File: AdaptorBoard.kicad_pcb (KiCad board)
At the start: 2 copper layers, 53.6 x 68.8 mm, 14 parts, among them J1 Conn_02x05_Odd_Even

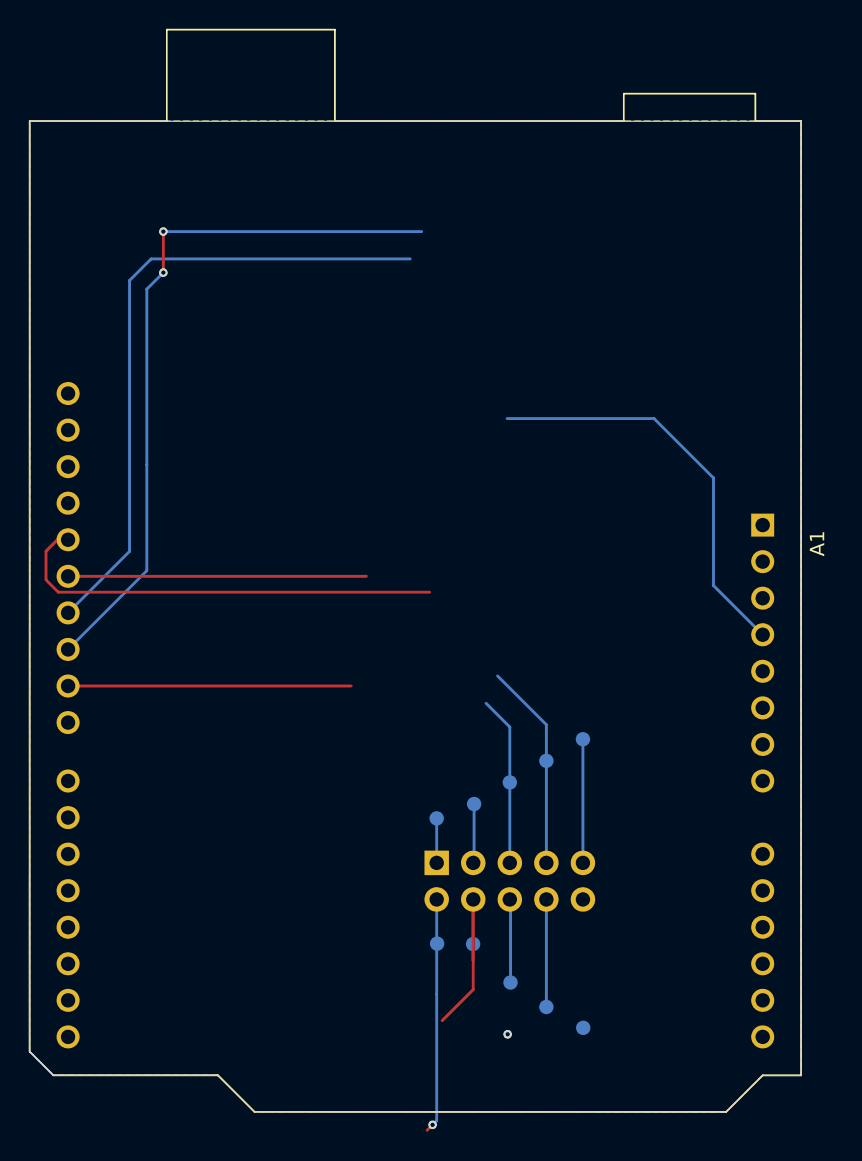
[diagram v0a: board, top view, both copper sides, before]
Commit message: Add EEPROM. Change from Reset Push to input. Assign footprints and more improvements.
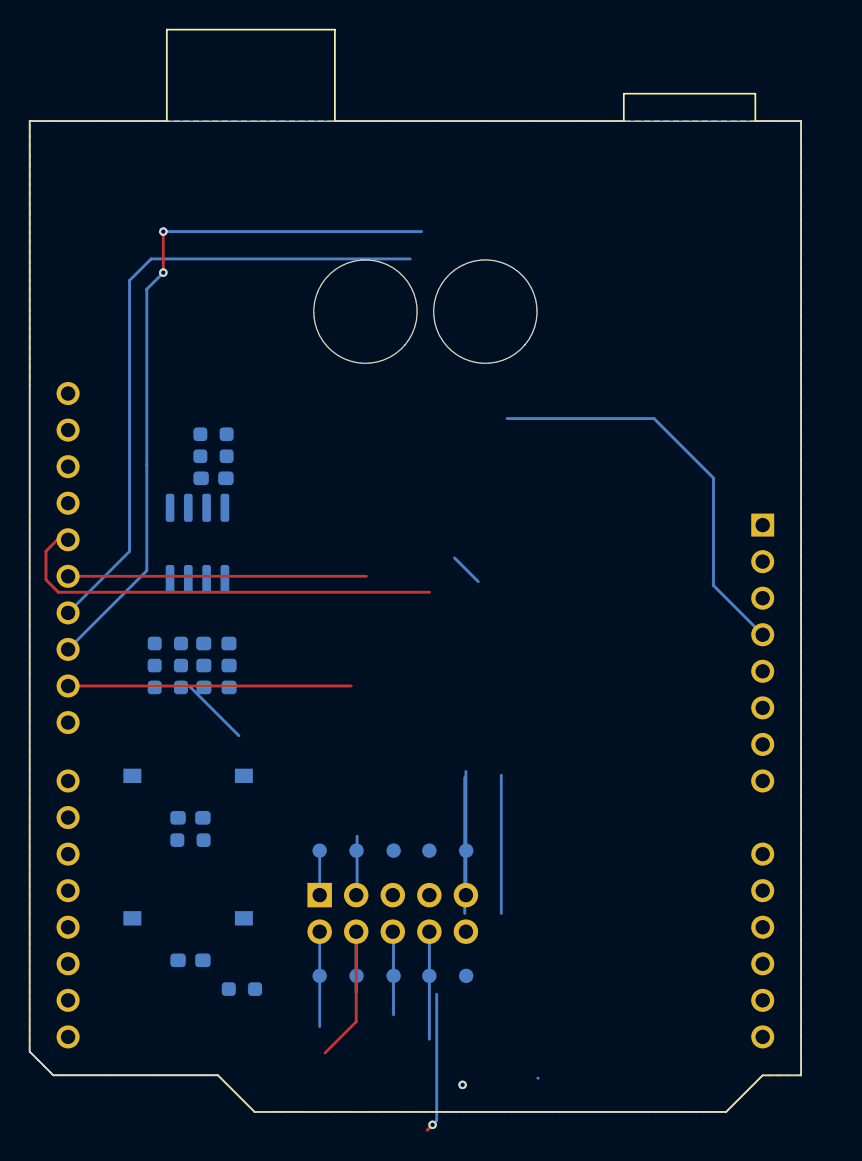
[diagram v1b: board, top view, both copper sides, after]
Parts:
- added C1: 100nF, Capacitor_SMD:C_0603_1608Metric_Pad1.08x0.95mm_HandSolder, B.Cu at (140.7, 130.3)
- added C2: 100nF, Capacitor_SMD:C_0603_1608Metric_Pad1.08x0.95mm_HandSolder, B.Cu at (140.7, 140.2)
- added C3: 100nF, Capacitor_SMD:C_0603_1608Metric_Pad1.08x0.95mm_HandSolder, B.Cu at (142.3, 106.7)
- added D1: LED, LED_SMD:LED_0603_1608Metric_Pad1.05x0.95mm_HandSolder, B.Cu at (142.5, 118.2)
- added D2: LED, LED_SMD:LED_0603_1608Metric_Pad1.05x0.95mm_HandSolder, B.Cu at (142.5, 119.8)
- added D3: LED, LED_SMD:LED_0603_1608Metric_Pad1.05x0.95mm_HandSolder, B.Cu at (142.5, 121.3)
- added R1: 1K, Resistor_SMD:R_0603_1608Metric_Pad0.98x0.95mm_HandSolder, B.Cu at (139.2, 121.3)
- added R2: 1K, Resistor_SMD:R_0603_1608Metric_Pad0.98x0.95mm_HandSolder, B.Cu at (139.2, 119.8)
- added R3: 1K, Resistor_SMD:R_0603_1608Metric_Pad0.98x0.95mm_HandSolder, B.Cu at (139.2, 118.2)
- added R4: 33K, Resistor_SMD:R_0603_1608Metric_Pad0.98x0.95mm_HandSolder, B.Cu at (140.7, 131.9)
- added R5: 33K, Resistor_SMD:R_0603_1608Metric_Pad0.98x0.95mm_HandSolder, B.Cu at (144.3, 142.2)
- added R6: 2.2K, Resistor_SMD:R_0603_1608Metric_Pad0.98x0.95mm_HandSolder, B.Cu at (142.3, 103.7)
- added R7: 2.2K, Resistor_SMD:R_0603_1608Metric_Pad0.98x0.95mm_HandSolder, B.Cu at (142.3, 105.2)
- added SW1: SW_Push, Button_Switch_SMD:SW_Tactile_SPST_NO_Straight_CK_PTS636Sx25SMTRLFS, B.Cu at (140.6, 127.4)
- added SW2: SW_Push, Button_Switch_SMD:SW_Tactile_SPST_NO_Straight_CK_PTS636Sx25SMTRLFS, B.Cu at (140.6, 137.3)
- added U1: 24LC1025, Package_SO:SOIC-8_3.9x4.9mm_P1.27mm, B.Cu at (141.2, 111.3)
- moved TP5 11.2 mm to (159.9, 132.6)
- moved TP4 10.2 mm to (157.3, 132.6)
- moved TP3 9.36 mm to (154.8, 132.6)
- moved TP10 8.90 mm to (159.9, 141.3)
- moved TP2 8.79 mm to (152.3, 132.6)
- moved TP6 8.46 mm to (149.7, 141.3)
- moved TP1 8.43 mm to (149.7, 132.6)
- moved J1 8.43 mm to (149.7, 135.7)
- moved TP9 8.41 mm to (157.3, 141.3)
- moved TP7 8.40 mm to (152.3, 141.3)
- moved TP8 8.13 mm to (154.8, 141.3)
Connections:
- A1 pad 21: unconnected-(A1-D6-Pad21) -> /PB_IN
- A1 pad 22: unconnected-(A1-D7-Pad22) -> /LED_ONE
- A1 pad 23: unconnected-(A1-D8-Pad23) -> /LED_TWO
- A1 pad 3: unconnected-(A1-~{RESET}-Pad3) -> /MCU_RESET
- A1 pad 31: unconnected-(A1-SDA/D2-Pad31) -> Net-(A1-SDA/D2)
- A1 pad 32: unconnected-(A1-SCL/D3-Pad32) -> Net-(A1-SCL/D3)
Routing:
- net /INT: track 36.0 -> 26.3 mm, vias 1 -> 0
- net /SO: track 34.3 -> 44.0 mm, vias 0 -> 1
- net /SI: track 57.0 -> 47.6 mm
- net +3.3V: track 36.9 -> 46.4 mm
- net /CS: track 64.1 -> 59.3 mm
- net Net-(D3-A): track 0.00 -> 4.79 mm
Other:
- outline, holes or cut-outs redrawn

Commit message: Fix position for push buttons' holes.
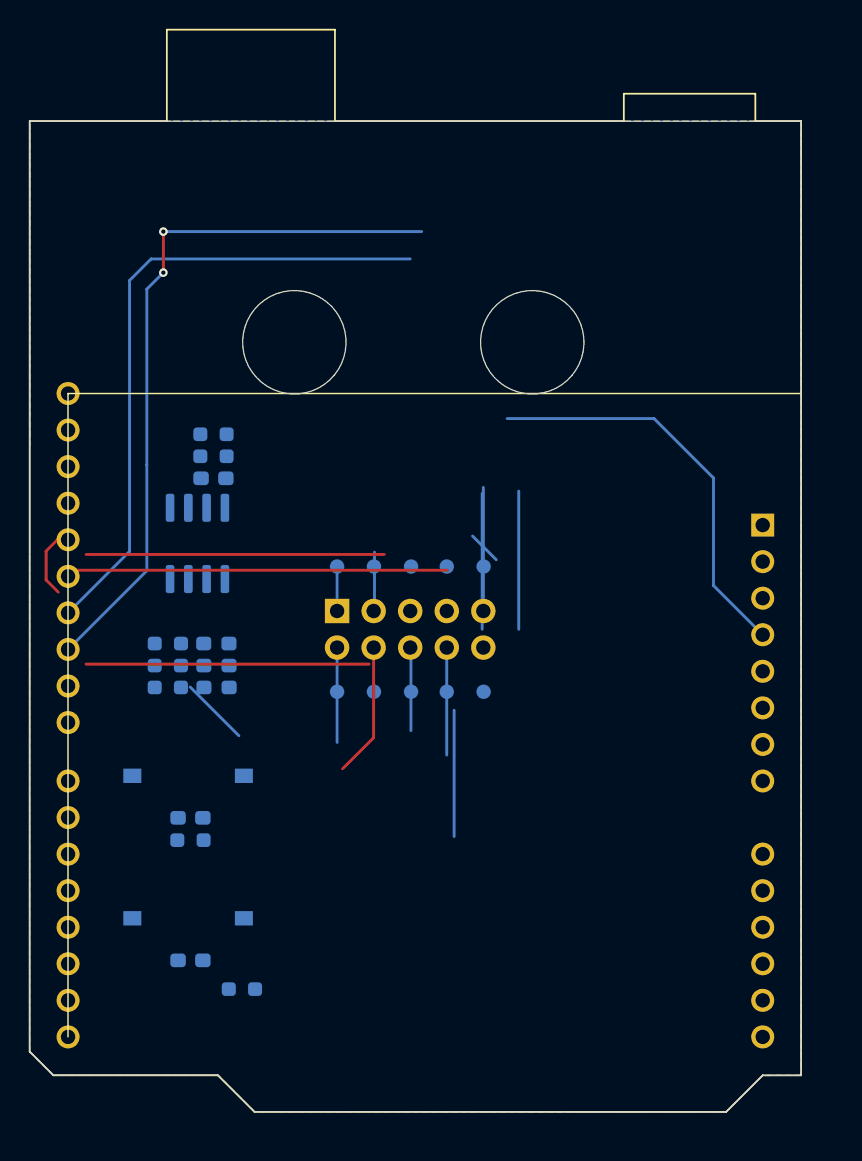
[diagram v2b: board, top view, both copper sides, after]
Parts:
- moved TP1 19.8 mm to (150.9, 112.9)
- moved TP10 19.8 mm to (161.1, 121.6)
- moved TP2 19.8 mm to (153.5, 112.9)
- moved TP3 19.8 mm to (156.1, 112.9)
- moved TP4 19.8 mm to (158.5, 112.9)
- moved TP5 19.8 mm to (161.1, 112.9)
- moved TP6 19.8 mm to (150.9, 121.6)
- moved TP7 19.8 mm to (153.5, 121.6)
- moved TP8 19.8 mm to (156.1, 121.6)
- moved TP9 19.8 mm to (158.5, 121.6)
- moved J1 19.8 mm to (150.9, 116.0)
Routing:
- net /SCK: track 37.0 -> 10.9 mm, vias 1 -> 0
- net /SO: track 44.0 -> 68.9 mm, vias 1 -> 0
- net /SI: track 47.6 -> 45.2 mm
- net +3.3V: track 46.4 -> 48.7 mm
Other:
- outline, holes or cut-outs redrawn
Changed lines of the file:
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@@
 		)
 		(property "Value" "Arduino_Leonardo"
-			(at 0 22.86 90)
+			(at -1.52 21.61 90)
 			(layer "F.Fab")
 			(effects
@@
 		)
 		(fp_text user "${REFERENCE}"
-			(at 0 20.32 90)
+			(at -1.52 20.32 90)
 			(layer "F.Fab")
 			(effects
@@
 	(footprint "TestPoint:TestPoint_Pad_D1.0mm"
 		(layer "B.Cu")
-		(at 149.71 141.31 180)
+		(at 150.92 121.57 180)
 		(descr "SMD pad as test Point, diameter 1.0mm")
 		(tags "test point SMD pad")
@@
 	(footprint "TestPoint:TestPoint_Pad_D1.0mm"
 		(layer "B.Cu")
-		(at 152.27 141.31)
+		(at 153.48 121.57)
 		(descr "SMD pad as test Point, diameter 1.0mm")
 		(tags "test point SMD pad")
@@
 	(footprint "TestPoint:TestPoint_Pad_D1.0mm"
 		(layer "B.Cu")
-		(at 154.85 141.31 180)
+		(at 156.06 121.57 180)
 		(descr "SMD pad as test Point, diameter 1.0mm")
 		(tags "test point SMD pad")
@@
 	(footprint "TestPoint:TestPoint_Pad_D1.0mm"
 		(layer "B.Cu")
-		(at 157.33 132.61 180)
+		(at 158.54 112.87 180)
 		(descr "SMD pad as test Point, diameter 1.0mm")
 		(tags "test point SMD pad")
@@
 	(footprint "TestPoint:TestPoint_Pad_D1.0mm"
 		(layer "B.Cu")
-		(at 157.33 141.31 180)
+		(at 158.54 121.57 180)
 		(descr "SMD pad as test Point, diameter 1.0mm")
 		(tags "test point SMD pad")
@@
 	(footprint "TestPoint:TestPoint_Pad_D1.0mm"
 		(layer "B.Cu")
-		(at 159.89 141.31 180)
+		(at 161.1 121.57 180)
 		(descr "SMD pad as test Point, diameter 1.0mm")
 		(tags "test point SMD pad")
@@
 	(footprint "Connector_PinHeader_2.54mm:PinHeader_2x05_P2.54mm_Vertical"
 		(layer "B.Cu")
-		(at 149.71 135.7 -90)
+		(at 150.92 115.96 -90)
 		(descr "Through hole straight pin header, 2x05, 2.54mm pitch, double rows")
 		(tags "Through hole pin header THT 2x05 2.54mm double row")
@@
 	(footprint "TestPoint:TestPoint_Pad_D1.0mm"
 		(layer "B.Cu")
-		(at 159.89 132.61 180)
+		(at 161.1 112.87 180)
 		(descr "SMD pad as test Point, diameter 1.0mm")
 		(tags "test point SMD pad")
@@
 	(footprint "TestPoint:TestPoint_Pad_D1.0mm"
 		(layer "B.Cu")
-		(at 152.27 132.61 180)
+		(at 153.48 112.87 180)
 		(descr "SMD pad as test Point, diameter 1.0mm")
 		(tags "test point SMD pad")
@@
 	(footprint "TestPoint:TestPoint_Pad_D1.0mm"
 		(layer "B.Cu")
-		(at 154.85 132.61 180)
+		(at 156.06 112.87 180)
 		(descr "SMD pad as test Point, diameter 1.0mm")
 		(tags "test point SMD pad")
@@
 	(footprint "TestPoint:TestPoint_Pad_D1.0mm"
 		(layer "B.Cu")
-		(at 149.71 132.61 180)
+		(at 150.92 112.87 180)
 		(descr "SMD pad as test Point, diameter 1.0mm")
 		(tags "test point SMD pad")
@@
 	)
 	(gr_line
+		(start 132.225 145.55)
+		(end 132.225 100.85)
+		(stroke
+			(width 0.1)
+			(type default)
+		)
+		(layer "F.SilkS")
+	)
+	(gr_line
+		(start 132.225 100.85)
+		(end 183.15 100.85)
+		(stroke
+			(width 0.1)
+			(type default)
+		)
+		(layer "F.SilkS")
+	)
+	(gr_line
 		(start 183.16 148.23)
 		(end 180.48 148.23)
@@
 	)
 	(gr_arc
-		(start 163.98008 97.459797)
-		(mid 158.46006 92.859821)
-		(end 163.98012 97.459749)
+		(start 167.23998 99.590091)
+		(mid 161.71996 94.990115)
+		(end 167.24002 99.590043)
 		(stroke
 			(width 0.05)
 			(type solid)
 		)
+		(locked yes)
 		(layer "Edge.Cuts")
 	)
@@
 	)
 	(gr_arc
-		(start 155.64996 97.460048)
-		(mid 150.13014 92.859672)
-		(end 155.65 97.46)
+		(start 150.71006 99.590048)
+		(mid 145.18992 94.989976)
+		(end 150.7101 99.59)
 		(stroke
 			(width 0.05)
 			(type solid)
 		)
+		(locked yes)
 		(layer "Edge.Cuts")
 	)
@@
 	)
 	(segment
-		(start 164.89 148.43)
-		(end 164.87 148.41)
-		(width 0.2)
-		(layer "B.Cu")
-		(net 1)
-	)
-	(segment
-		(start 160.73 113.92)
-		(end 159.08 112.27)
-		(width 0.2)
-		(layer "B.Cu")
-		(net 4)
-	)
-	(segment
 		(start 156 91.5)
 		(end 138 91.5)
@@
 	)
 	(segment
-		(start 159.64 148.88)
-		(end 159.489 149.031)
-		(width 0.2)
-		(layer "F.Cu")
-		(net 10)
-	)
-	(segment
-		(start 157.349 114.651)
-		(end 131.551 114.651)
-		(width 0.2)
-		(layer "F.Cu")
-		(net 10)
-	)
-	(via
-		(at 159.64 148.88)
-		(size 0.6)
-		(drill 0.3)
-		(layers "F.Cu" "B.Cu")
-		(net 10)
-	)
-	(segment
-		(start 159.64 148.88)
-		(end 159.74 148.78)
+		(start 156.05 118.55)
+		(end 156.05 124.27)
 		(width 0.2)
 		(layer "B.Cu")
@@
 	)
 	(segment
-		(start 154.84 138.29)
-		(end 154.84 144.01)
+		(start 156 118.5)
+		(end 156 118.47)
 		(width 0.2)
 		(layer "B.Cu")
@@
 	)
 	(segment
-		(start 154.79 138.24)
-		(end 154.79 138.21)
+		(start 156 118.5)
+		(end 156.05 118.55)
 		(width 0.2)
 		(layer "B.Cu")
@@
 	)
 	(segment
-		(start 154.79 138.24)
-		(end 154.84 138.29)
+		(start 161.98 112.4)
+		(end 160.33 110.75)
 		(width 0.2)
 		(layer "B.Cu")
-		(net 10)
+		(net 21)
 	)
 	(segment
-		(start 159.79 136.97)
-		(end 159.79 127.53)
+		(start 161 117.23)
+		(end 161 107.79)
 		(width 0.2)
 		(layer "B.Cu")
@@
 	)
 	(segment
-		(start 159.87 127.11)
-		(end 159.87 135.7)
+		(start 161.08 107.37)
+		(end 161.08 115.96)
 		(width 0.2)
 		(layer "B.Cu")
@@
 	)
 	(segment
-		(start 152.95 113.55)
-		(end 132.23 113.55)
+		(start 154.2 112.03)
+		(end 133.48 112.03)
 		(width 0.2)
 		(layer "F.Cu")
@@
 	)
 	(segment
-		(start 152.25 144.5)
-		(end 150.09 146.66)
+		(start 153.46 124.76)
+		(end 151.3 126.92)
 		(width 0.2)
 		(layer "F.Cu")
@@
 	)
 	(segment
-		(start 152.25 138.24)
-		(end 152.25 144.5)
+		(start 153.46 118.5)
+		(end 153.46 124.76)
 		(width 0.2)
 		(layer "F.Cu")
@@
 	)
 	(segment
-		(start 157.555 151.655)
-		(end 157.17 152.04)
+		(start 158.599 113.131)
+		(end 132.801 113.131)
 		(width 0.2)
 		(layer "F.Cu")
 		(net 25)
 	)
-	(via
-		(at 157.555 151.655)
-		(size 0.6)
-		(drill 0.3)
-		(layers "F.Cu" "B.Cu")
-		(net 25)
-	)
-	(segment
-		(start 157.84 142.59)
-		(end 157.84 151.37)
-		(width 0.2)
-		(layer "B.Cu")
-		(net 25)
-	)
 	(segment
-		(start 152.25 138.24)
-		(end 152.24 138.25)
+		(start 159.05 122.85)
+		(end 159.05 131.63)
 		(width 0.2)
 		(layer "B.Cu")
@@
 	)
 	(segment
-		(start 152.24 138.25)
-		(end 152.24 142.51)
+		(start 153.46 118.5)
+		(end 153.45 118.51)
 		(width 0.2)
 		(layer "B.Cu")
@@
 	)
 	(segment
-		(start 157.84 151.37)
-		(end 157.555 151.655)
+		(start 153.45 118.51)
+		(end 153.45 122.77)
 		(width 0.2)
 		(layer "B.Cu")
@@
 	)
 	(segment
-		(start 162.33 136.97)
-		(end 162.33 127.37)
+		(start 163.54 117.23)
+		(end 163.54 107.63)
 		(width 0.2)
 		(layer "B.Cu")
@@
 	)
 	(segment
-		(start 151.9 121.17)
-		(end 132.23 121.17)
+		(start 153.15 119.65)
+		(end 133.48 119.65)
 		(width 0.2)
 		(layer "F.Cu")
@@
 	)
 	(segment
-		(start 149.71 138.24)
-		(end 149.71 144.83)
+		(start 150.92 118.5)
+		(end 150.92 125.09)
 		(width 0.2)
 		(layer "B.Cu")
@@
 	)
 	(segment
-		(start 152.31 135.64)
-		(end 152.31 131.61)
+		(start 153.52 115.9)
+		(end 153.52 111.87)
 		(width 0.2)
 		(layer "B.Cu")
@@
 	)
 	(segment
-		(start 152.25 135.7)
-		(end 152.31 135.64)
+		(start 153.46 115.96)
+		(end 153.52 115.9)
 		(width 0.2)
 		(layer "B.Cu")
@@
 	)
 	(segment
-		(start 157.33 138.24)
-		(end 157.24 138.33)
+		(start 158.54 118.5)
+		(end 158.45 118.59)
 		(width 0.2)
 		(layer "B.Cu")
@@
 	)
 	(segment
-		(start 157.33 145.71)
-		(end 157.33 138.24)
+		(start 158.54 125.97)
+		(end 158.54 118.5)
 		(width 0.2)
 		(layer "B.Cu")
@@
 	)
 	(segment
-		(start 149.71 132.61)
-		(end 149.71 135.7)
+		(start 150.92 112.87)
+		(end 150.92 115.96)
 		(width 0.2)
 		(layer "B.Cu")

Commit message: Finalize the PCB Design
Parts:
- moved G*** 20.8 mm to (176.0, 86.2)
- moved REF** 8.42 mm to (173.9, 96.1)
- moved R5 4.08 mm to (140.8, 140.2)
- moved R4 1.55 mm to (140.8, 130.3)
- moved C1 1.55 mm to (140.8, 131.9)
- moved C2 1.52 mm to (140.8, 141.8)
- moved R3 0.17 mm to (139.2, 118.0), turned to 0 degrees
- moved D1 0.17 mm to (142.5, 118.0)
- moved R2 0.10 mm to (139.2, 119.7), turned to 0 degrees
- moved D2 0.10 mm to (142.6, 119.7)
- turned R1 to 0 degrees
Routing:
- net +3.3V: track 48.7 -> 172.7 mm, vias 0 -> 1
- net /MCU_RESET: track 0.00 -> 67.6 mm, vias 0 -> 1
- net /SO: track 68.9 -> 26.4 mm
- net /CS: track 59.3 -> 36.1 mm, vias 2 -> 0
- net /SCK: track 10.9 -> 31.7 mm, vias 0 -> 1
- net Net-(A1-SCL/D3): track 0.00 -> 18.3 mm
- net /PB_IN: track 0.00 -> 17.7 mm
- net Net-(A1-SDA/D2): track 0.00 -> 14.3 mm
- net /SI: track 45.2 -> 31.3 mm, vias 0 -> 1
- net /LED_ONE: track 0.00 -> 12.6 mm
- net /LED_TWO: track 0.00 -> 10.1 mm
- net /RESET: track 7.60 -> 3.20 mm
- net Net-(D3-A): track 4.79 -> 1.59 mm
- net /INT: track 26.3 -> 23.3 mm, vias 0 -> 1
- net GND: track 0.00 -> 2.63 mm, vias 0 -> 554
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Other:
- board text added: "03/04/2026 Ethernet ENC28J60 Shield V2"
- board text removed: "10/03/2026 Ethernet ENC28J60 Shield V2"
